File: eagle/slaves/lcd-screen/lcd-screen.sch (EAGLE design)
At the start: 29 parts, among them CON1 SPI, IC1 MCP1703CB, J1 RJ12RIGHTANGLE-I2C, J2 RJ12RIGHTANGLE-I2C, J3 RJ12RIGHTANGLE-I2C, U1 ATMEGA328P_TQFP, X1 8MHz

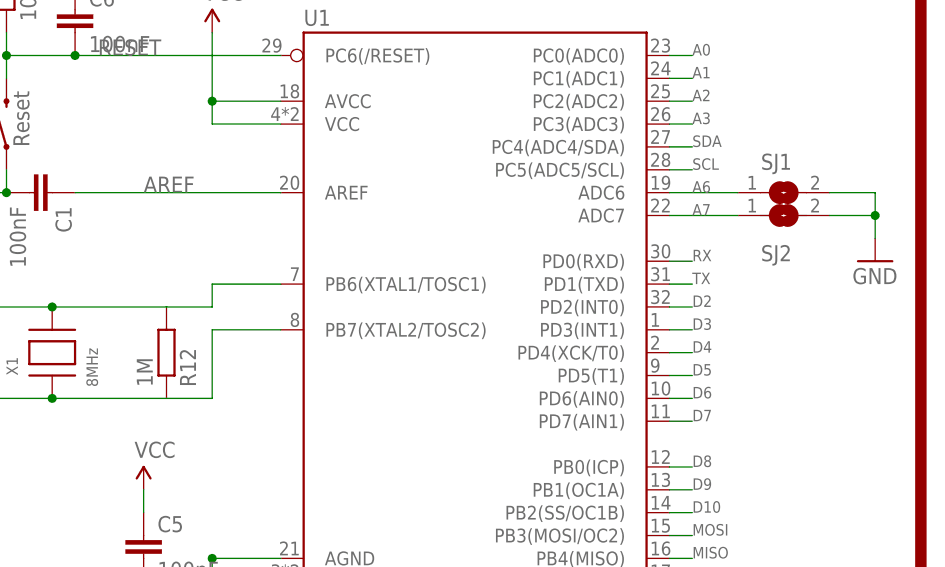
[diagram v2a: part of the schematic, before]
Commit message: submitted lcd-screen design
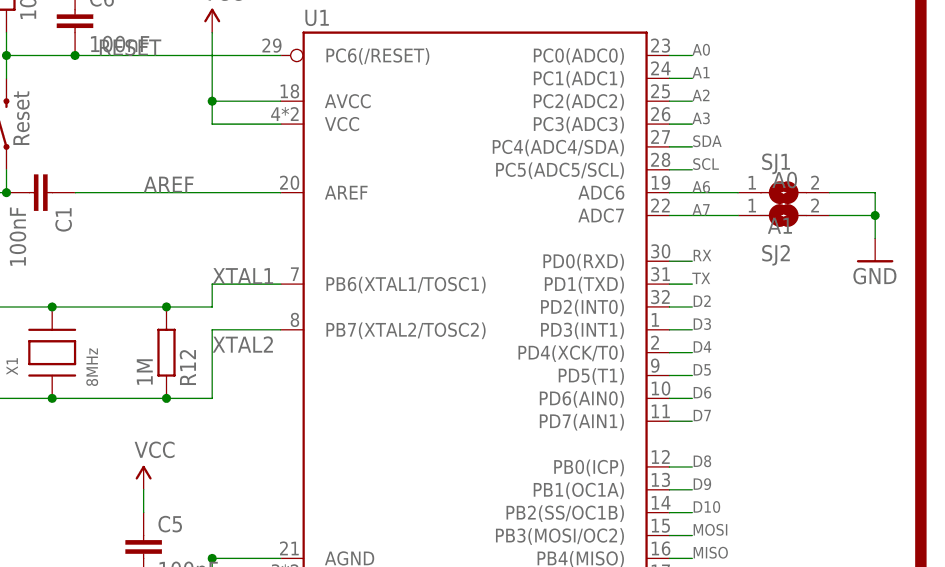
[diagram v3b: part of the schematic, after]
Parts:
- SJ1: value (none) -> A0
- SJ2: value (none) -> A1
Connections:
- removed net N$42: C8.2, R12.2, U1.PB6(XTAL1/TOSC1), X1.P$2
- new net XTAL2: C7.2, R12.1, U1.PB7(XTAL2/TOSC2), X1.P$1
- net XTAL1: now also C8.2, R12.2, U1.PB6(XTAL1/TOSC1), X1.P$2; no longer C7.2, R12.1, U1.PB7(XTAL2/TOSC2), X1.P$1
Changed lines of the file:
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@@
 <attribute name="MPN" value="621-1N5819HW-F"/>
 </part>
-<part name="SJ1" library="jumper" library_urn="urn:adsk.eagle:library:252" deviceset="SJ" device="" package3d_urn="urn:adsk.eagle:package:15471/1"/>
-<part name="SJ2" library="jumper" library_urn="urn:adsk.eagle:library:252" deviceset="SJ" device="" package3d_urn="urn:adsk.eagle:package:15471/1"/>
+<part name="SJ1" library="jumper" library_urn="urn:adsk.eagle:library:252" deviceset="SJ" device="" package3d_urn="urn:adsk.eagle:package:15471/1" value="A0"/>
+<part name="SJ2" library="jumper" library_urn="urn:adsk.eagle:library:252" deviceset="SJ" device="" package3d_urn="urn:adsk.eagle:package:15471/1" value="A1"/>
 <part name="GND13" library="SparkFun" deviceset="GND" device=""/>
 <part name="C7" library="rcl" library_urn="urn:adsk.eagle:library:334" deviceset="C-EU" device="C0805K" package3d_urn="urn:adsk.eagle:package:23681/2" value="18pF">
@@
 <instance part="SJ1" gate="1" x="193.04" y="116.84" smashed="yes">
 <attribute name="NAME" x="190.5" y="119.38" size="1.778" layer="95"/>
-<attribute name="VALUE" x="190.5" y="113.03" size="1.778" layer="96"/>
+<attribute name="VALUE" x="191.77" y="117.348" size="1.778" layer="96"/>
 </instance>
 <instance part="SJ2" gate="1" x="193.04" y="114.3" smashed="yes">
 <attribute name="NAME" x="190.5" y="109.22" size="1.778" layer="95"/>
-<attribute name="VALUE" x="190.5" y="110.49" size="1.778" layer="96"/>
+<attribute name="VALUE" x="191.262" y="112.268" size="1.778" layer="96"/>
 </instance>
 <instance part="GND13" gate="1" x="203.2" y="109.22"/>
@@
 </segment>
 </net>
-<net name="XTAL1" class="0">
+<net name="XTAL2" class="0">
 <segment>
 <pinref part="C7" gate="G$1" pin="2"/>
@@
 <wire x1="129.54" y1="101.6" x2="129.54" y2="93.98" width="0.1524" layer="91"/>
 <wire x1="129.54" y1="93.98" x2="124.46" y2="93.98" width="0.1524" layer="91"/>
-</segment>
-</net>
-<net name="N$42" class="0">
+<junction x="124.46" y="93.98"/>
+<label x="129.54" y="99.06" size="1.778" layer="95"/>
+</segment>
+</net>
+<net name="XTAL1" class="0">
 <segment>
 <pinref part="C8" gate="G$1" pin="2"/>
@@
 <pinref part="U1" gate="U1" pin="PB6(XTAL1/TOSC1)"/>
 <wire x1="129.54" y1="106.68" x2="137.16" y2="106.68" width="0.1524" layer="91"/>
+<junction x="124.46" y="104.14"/>
+<label x="129.54" y="106.68" size="1.778" layer="95"/>
 </segment>
 </net>
@@
 </sheet>
 </sheets>
-<errors>
-</errors>
 </schematic>
 </drawing>
